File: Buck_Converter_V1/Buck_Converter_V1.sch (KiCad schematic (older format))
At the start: 6 parts

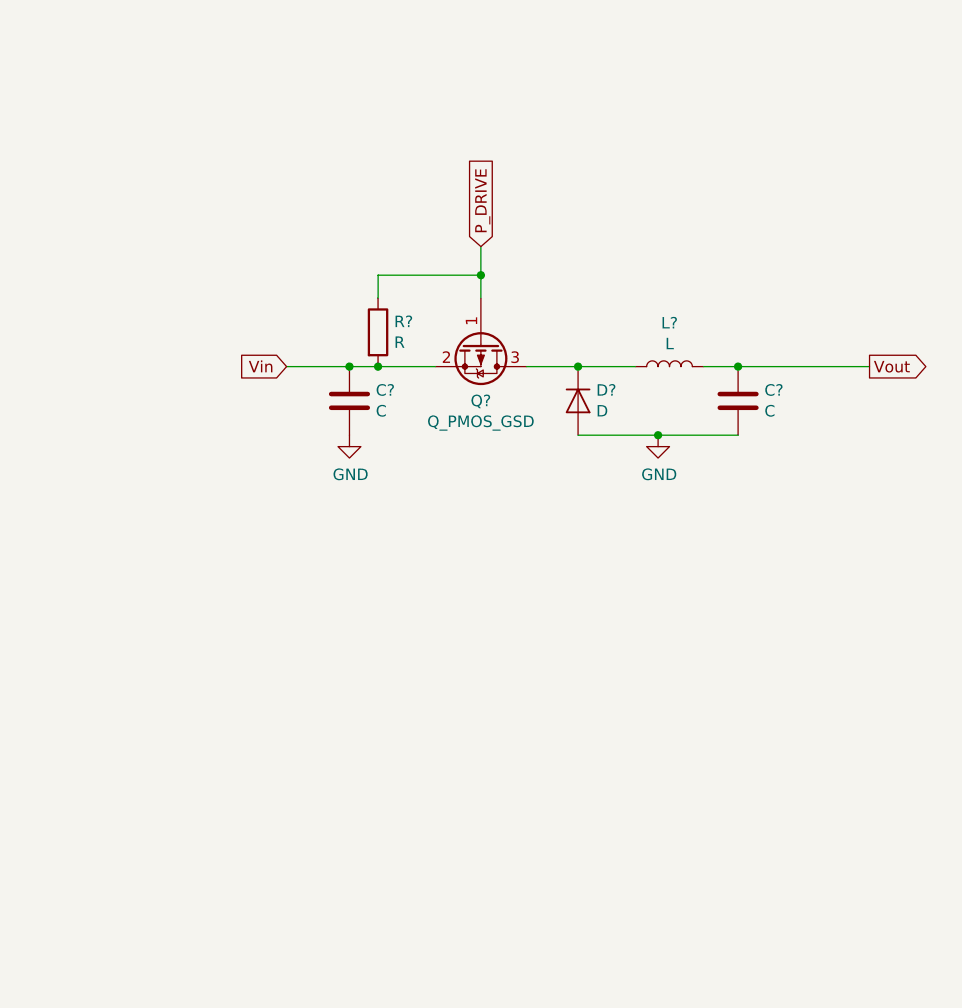
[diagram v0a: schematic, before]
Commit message: Added controller circuit
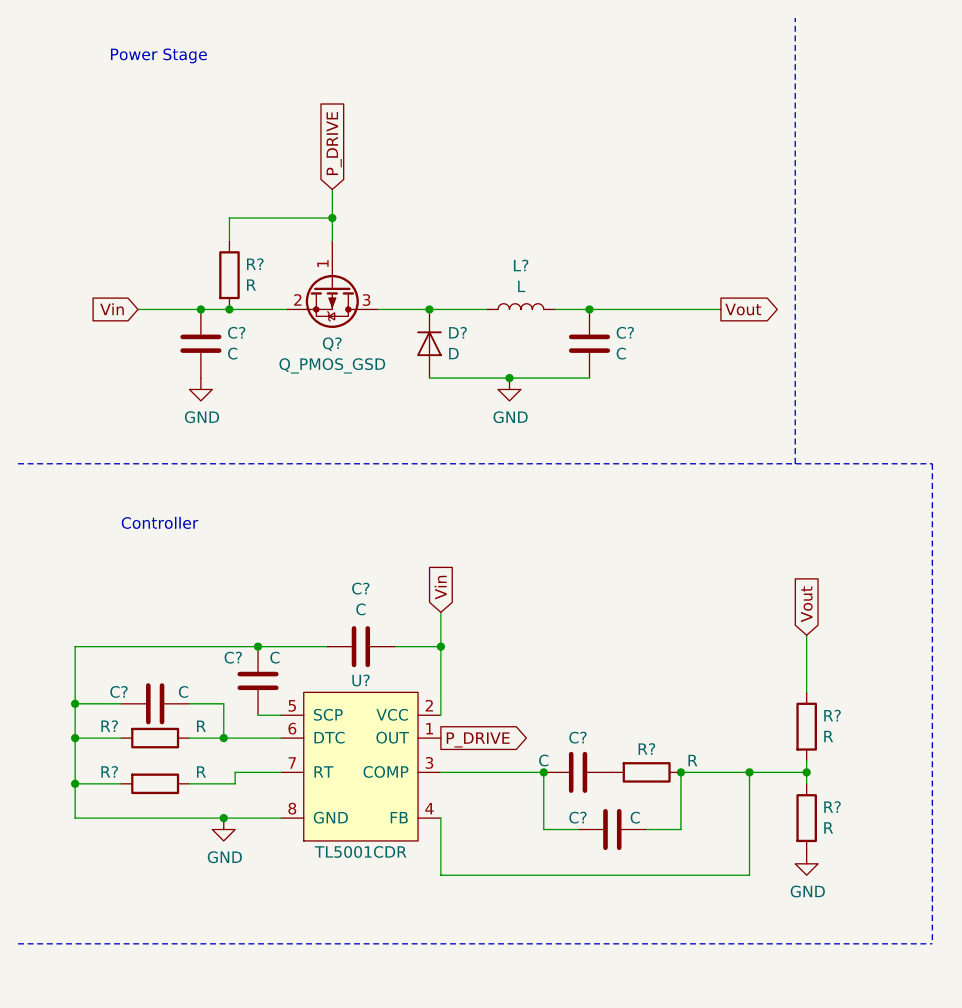
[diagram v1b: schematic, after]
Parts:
- added C? (x5): C, symbol Device:C
- added R? (x5): R, symbol Device:R
- added U?: TL5001CDR, symbol Project_Libary:TL5001CDR
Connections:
- net GND: now also C?.1, C?.2, C?.2, R?.2, R?.2, R?.2, U?.8 (GND)
- net P_DRIVE: now also U?.1 (OUT)
- net Vin: now also C?.1, U?.2 (VCC)
- net Vout: now also R?.1
- new net: C?.2, C?.2, U?.3 (COMP)
- new net: C?.1, R?.1, R?.1, R?.2, U?.4 (FB)
- new net: C?.2, U?.5 (SCP)
- new net: C?.1, R?.1, U?.6 (DTC)
- new net: R?.1, U?.7 (RT)
- new net: C?.1, R?.2
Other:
- note added: "Controller"
- note added: "Power Stage"
- moved on the sheet: C?, D?, L?, Q?, R?

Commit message: Updated some component values
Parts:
- removed D?: D, symbol Device:D
- added D?: D_Schottky, symbol Device:D_Schottky
- C?: symbol Device:C -> Device:CP1
- C?: value C -> 100uF; symbol Device:C -> Device:CP1
- C?: value C -> 0.1uF
- C?: value C -> 1uF
- C?: value C -> NC
- R?: value R -> 3k
- R?: value R -> NC
- R?: value R -> 25k
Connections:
- net GND: now also D?.2 (A)
- net at L?.1, Q?.3 (D): now also D?.1 (K)
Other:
- note added: "RT chosen to be 25k for roughly 300kHZ switching frequency"
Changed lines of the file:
@@
 $EndComp
 $Comp
-L Device:C C?
+L Device:CP1 C?
 U 1 1 5C184B5B
 P 3000 1975
@@
 	1    3000 1975
 	1    0    0    -1
-$EndComp
-$Comp
-L Device:D D?
-U 1 1 5C184C28
-P 2300 1975
-F 0 "D?" V 2254 2054 50  0000 L CNN
-F 1 "D" V 2345 2054 50  0000 L CNN
-F 2 "" H 2300 1975 50  0001 C CNN
-F 3 "~" H 2300 1975 50  0001 C CNN
-	1    2300 1975
-	0    1    1    0
 $EndComp
 $Comp
@@
 P 1425 1675
 F 0 "R?" H 1495 1721 50  0000 L CNN
-F 1 "R" H 1495 1630 50  0000 L CNN
+F 1 "3k" H 1495 1630 50  0000 L CNN
 F 2 "" V 1355 1675 50  0001 C CNN
 F 3 "~" H 1425 1675 50  0001 C CNN
@@
 	1425 1825 1300 1825
 $Comp
-L Device:C C?
+L Device:CP1 C?
 U 1 1 5C185AC1
 P 1300 1975
 F 0 "C?" H 1415 2021 50  0000 L CNN
-F 1 "C" H 1415 1930 50  0000 L CNN
+F 1 "100uF" H 1415 1930 50  0000 L CNN
 F 2 "" H 1338 1825 50  0001 C CNN
 F 3 "~" H 1300 1975 50  0001 C CNN
@@
 Text GLabel 1025 1825 0    50   Input ~ 0
 Vin
-Wire Wire Line
-	2075 1825 2300 1825
-Connection ~ 2300 1825
-Wire Wire Line
-	2300 1825 2550 1825
 Wire Wire Line
 	2850 1825 3000 1825
@@
 P 2000 3300
 F 0 "C?" V 1748 3300 50  0000 C CNN
-F 1 "C" V 1839 3300 50  0000 C CNN
+F 1 "0.1uF" V 1839 3300 50  0000 C CNN
 F 2 "" H 2038 3150 50  0001 C CNN
 F 3 "~" H 2000 3300 50  0001 C CNN
@@
 P 1550 3450
 F 0 "C?" H 1400 3550 50  0000 L CNN
-F 1 "C" H 1600 3550 50  0000 L CNN
+F 1 "1uF" H 1600 3550 50  0000 L CNN
 F 2 "" H 1588 3300 50  0001 C CNN
 F 3 "~" H 1550 3450 50  0001 C CNN
@@
 $Comp
 L Device:R R?
-U 1 1 5C18A825
-P 1100 3700
-F 0 "R?" V 1050 3500 50  0000 C CNN
-F 1 "R" V 1050 3900 50  0000 C CNN
-F 2 "" V 1030 3700 50  0001 C CNN
-F 3 "~" H 1100 3700 50  0001 C CNN
-	1    1100 3700
-	0    1    1    0
-$EndComp
-$Comp
-L Device:R R?
 U 1 1 5C18A87B
 P 1100 3900
 F 0 "R?" V 1050 3700 50  0000 C CNN
-F 1 "R" V 1050 4100 50  0000 C CNN
+F 1 "25k" V 1050 4100 50  0000 C CNN
 F 2 "" V 1030 3900 50  0001 C CNN
 F 3 "~" H 1100 3900 50  0001 C CNN
@@
 	0    1    1    0
 $EndComp
-$Comp
-L Device:C C?
-U 1 1 5C18AA6D
-P 1100 3550
-F 0 "C?" V 1050 3350 50  0000 L CNN
-F 1 "C" V 1050 3650 50  0000 L CNN
-F 2 "" H 1138 3400 50  0001 C CNN
-F 3 "~" H 1100 3550 50  0001 C CNN
-	1    1100 3550
-	0    1    1    0
-$EndComp
-Wire Wire Line
-	1250 3700 1400 3700
-Wire Wire Line
-	1250 3550 1400 3550
-Wire Wire Line
-	1400 3550 1400 3700
-Wire Wire Line
-	1650 3700 1400 3700
-Connection ~ 1400 3700
 Wire Wire Line
 	1250 3900 1450 3900
@@
 Wire Wire Line
 	1550 3300 750  3300
-Wire Wire Line
-	750  3300 750  3550
 Wire Wire Line
 	750  4050 1400 4050
 Connection ~ 1550 3300
-Wire Wire Line
-	950  3550 750  3550
-Connection ~ 750  3550
-Wire Wire Line
-	750  3550 750  3700
-Wire Wire Line
-	950  3700 750  3700
-Connection ~ 750  3700
-Wire Wire Line
-	750  3700 750  3900
 Wire Wire Line
 	950  3900 750  3900
@@
 Wire Notes Line
 	4500 2500 4500 4600
+Wire Wire Line
+	750  3700 750  3900
+Connection ~ 750  3700
+Wire Wire Line
+	950  3700 750  3700
+Wire Wire Line
+	750  3550 750  3700
+Wire Wire Line
+	750  3300 750  3550
+Connection ~ 750  3550
+Wire Wire Line
+	950  3550 750  3550
+Wire Wire Line
+	1250 3550 1400 3550
+Wire Wire Line
+	1400 3550 1400 3700
+Wire Wire Line
+	1650 3700 1400 3700
+Connection ~ 1400 3700
+Wire Wire Line
+	1250 3700 1400 3700
+$Comp
+L Device:R R?
+U 1 1 5C18A825
+P 1100 3700
+F 0 "R?" V 1050 3500 50  0000 C CNN
+F 1 "NC" V 1050 3900 50  0000 C CNN
+F 2 "" V 1030 3700 50  0001 C CNN
+F 3 "~" H 1100 3700 50  0001 C CNN
+	1    1100 3700
+	0    1    1    0
+$EndComp
+$Comp
+L Device:C C?
+U 1 1 5C18AA6D
+P 1100 3550
+F 0 "C?" V 1050 3350 50  0000 L CNN
+F 1 "NC" V 1050 3650 50  0000 L CNN
+F 2 "" H 1138 3400 50  0001 C CNN
+F 3 "~" H 1100 3550 50  0001 C CNN
+	1    1100 3550
+	0    1    1    0
+$EndComp
+Wire Wire Line
+	2075 1825 2300 1825
+$Comp
+L Device:D_Schottky D?
+U 1 1 5C1F0F49
+P 2300 1975
+F 0 "D?" V 2254 2054 50  0000 L CNN
+F 1 "D_Schottky" V 2345 2054 50  0000 L CNN
+F 2 "" H 2300 1975 50  0001 C CNN
+F 3 "~" H 2300 1975 50  0001 C CNN
+	1    2300 1975
+	0    1    1    0
+$EndComp
+Connection ~ 2300 1825
+Wire Wire Line
+	2300 1825 2550 1825
+Text Notes 700  4475 0    50   ~ 0
+RT chosen to be 25k for roughly 300kHZ switching frequency
 $EndSCHEMATC

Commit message: Changed values for dead time control
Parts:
- C?: value NC -> 0.1uF
- R?: value NC -> 56k
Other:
- note added: "DTC component values chosen for max duty cycle of 90%"
- note added: "SCP value chosen for 70ms reaction time"
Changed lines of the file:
@@
 $EndComp
 Wire Notes Line
-	500  4600 4500 4600
+	500  4800 4500 4800
 Wire Notes Line
 	500  2500 4500 2500
-Wire Notes Line
-	4500 2500 4500 4600
 Wire Wire Line
 	750  3700 750  3900
@@
 P 1100 3700
 F 0 "R?" V 1050 3500 50  0000 C CNN
-F 1 "NC" V 1050 3900 50  0000 C CNN
+F 1 "56k" V 1050 3900 50  0000 C CNN
 F 2 "" V 1030 3700 50  0001 C CNN
 F 3 "~" H 1100 3700 50  0001 C CNN
@@
 P 1100 3550
 F 0 "C?" V 1050 3350 50  0000 L CNN
-F 1 "NC" V 1050 3650 50  0000 L CNN
+F 1 "0.1uF" V 1050 3650 50  0000 L CNN
 F 2 "" H 1138 3400 50  0001 C CNN
 F 3 "~" H 1100 3550 50  0001 C CNN
@@
 Text Notes 700  4475 0    50   ~ 0
 RT chosen to be 25k for roughly 300kHZ switching frequency
+Text Notes 700  4600 0    50   ~ 0
+DTC component values chosen for max duty cycle of 90%
+Text Notes 700  4725 0    50   ~ 0
+SCP value chosen for 70ms reaction time
+Wire Notes Line
+	4500 2500 4500 4800
 $EndSCHEMATC
